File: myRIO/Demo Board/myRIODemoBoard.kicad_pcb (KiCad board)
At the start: 2 copper layers, 45.7 x 38.1 mm, 5 parts, among them U1 MXP

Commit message: Small updates to footprints, schematic, etc.
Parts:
- moved RV1 3.57 mm to (141.2, 77.2)
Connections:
- net N-000001 renamed f
- net N-0000014 renamed dp
- net N-000002 renamed e
- net N-000003 renamed d
- net N-000004 renamed c
- net N-000005 renamed b
- net N-000006 renamed a
- net N-000007 renamed g
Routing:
- net N-000009: track 22.4 -> 26.0 mm
- net +5V: track 24.4 -> 28.1 mm
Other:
- board text added: "myRIO Demo Board Rev 1.0 SK"

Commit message: Prototype Order of Rev 1.0
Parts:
- 7SEG1: value 7SEGMENTS -> 7-Segment Display
- RV1: value POT -> Potentiometer
- U1: value MXP -> NI myRIO MXP
- moved C1 19.2 mm to (143.5, 83.8), turned to 90 degrees
- moved R1 17.8 mm to (132.1, 81.3), turned to 90 degrees
- moved 7SEG1 3.81 mm to (116.8, 72.4), turned to 90 degrees
- moved RV1 3.23 mm to (143.5, 74.9), turned to 180 degrees
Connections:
- RV1 pad 3: +5V -> +3.3V
- U1 pad 1: +5V -> (no net)
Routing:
- net b: track 20.6 -> 51.5 mm
- net N-000006: track 14.8 -> 44.0 mm
- net +5V: track 28.1 -> 0.00 mm
- net N-0000018: track 36.2 -> 61.4 mm
- net dp: track 40.8 -> 15.8 mm
- net a: track 27.8 -> 52.6 mm
- net d: track 49.6 -> 25.5 mm
- net e: track 47.8 -> 26.5 mm
- net g: track 15.1 -> 33.1 mm
- net f: track 15.1 -> 30.6 mm
- net N-0000021: track 26.0 -> 12.7 mm
- net GND: track 9.20 -> 21.4 mm, vias 1 -> 0
- net c: track 31.4 -> 21.9 mm
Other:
- board text added: "Capacitor"
- board text added: "Design Real Systems, Fast"
- board text added: "NI myRIO"
- board text added: "Resistor"
- board text added: "Rev 1.0 - SK"
- board text removed: "myRIO Demo Board Rev 1.0 SK"

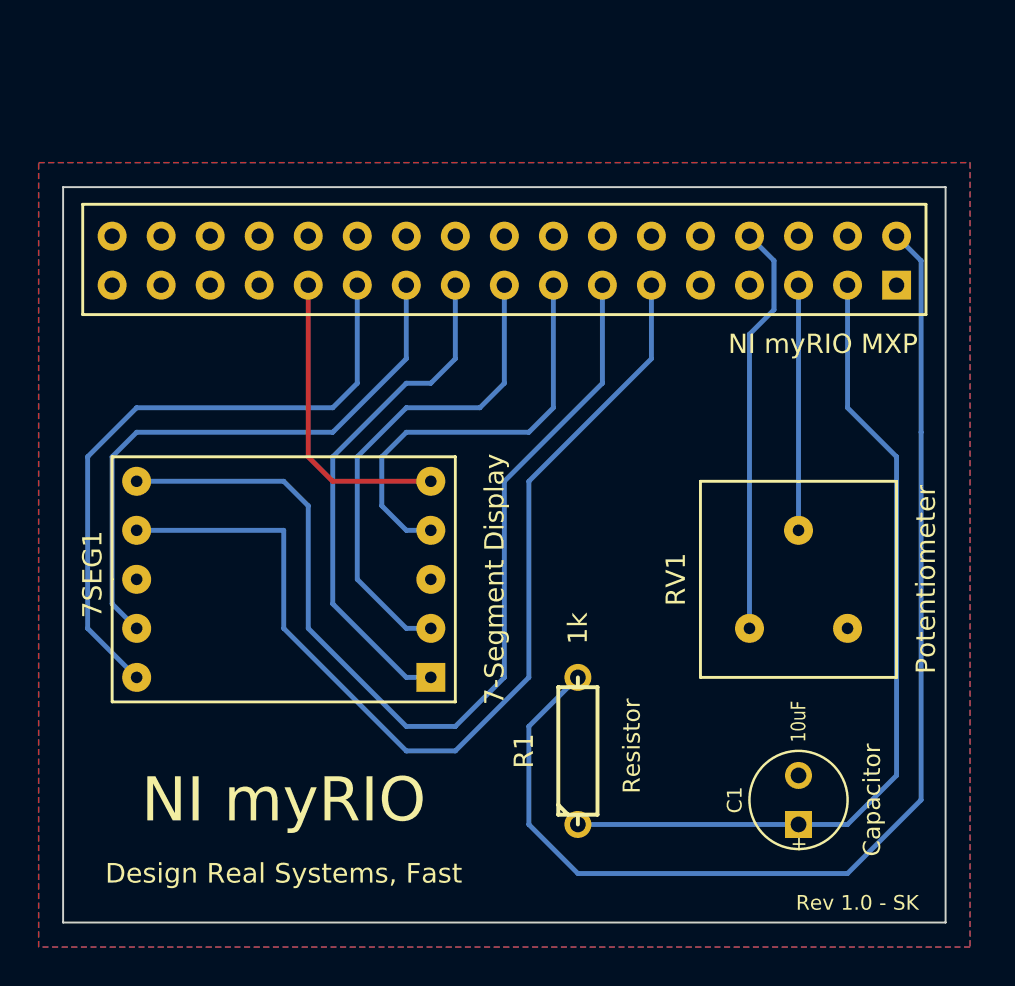
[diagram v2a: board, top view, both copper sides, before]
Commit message: Updated myRIO Demo Board to Rev 1.1. Modified component IDs for manufacturing. Adjusted silk screen.
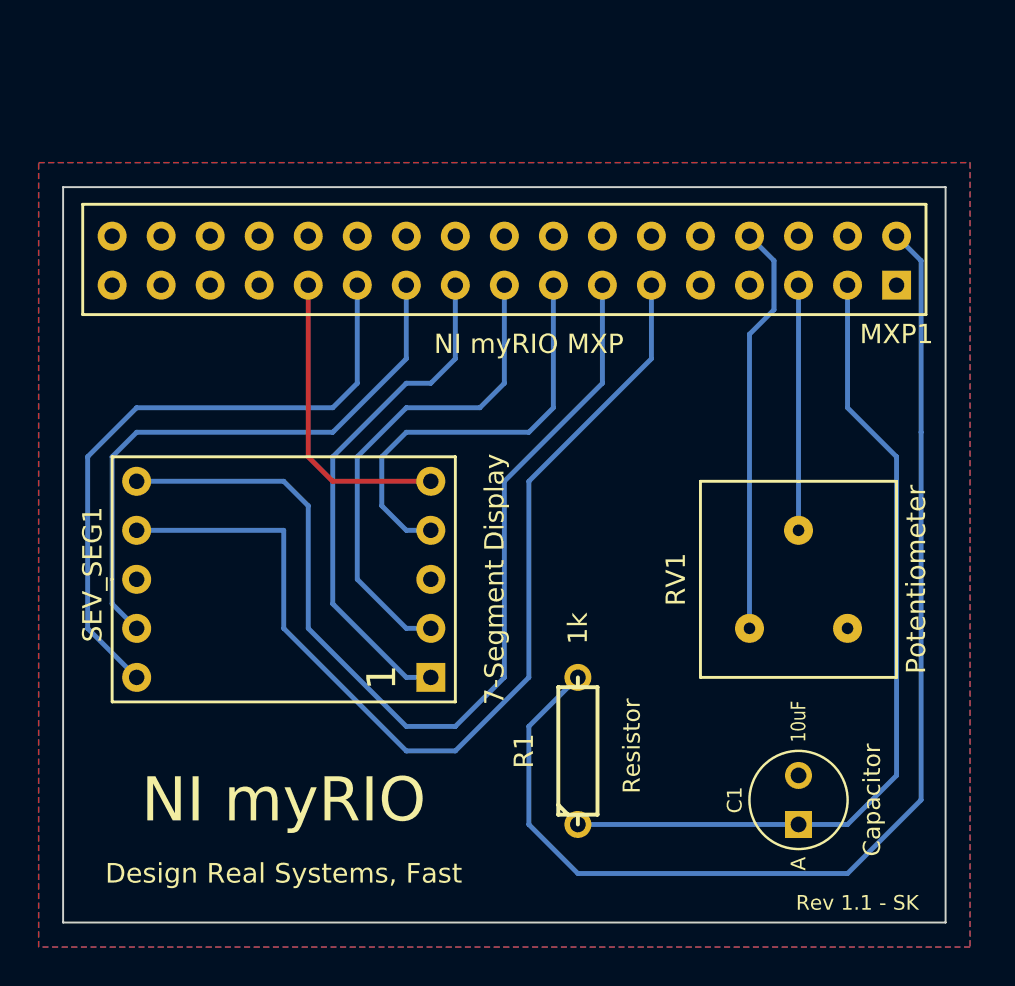
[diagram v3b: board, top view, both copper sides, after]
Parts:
- renumbered U1 to MXP1, 7SEG1 to SEV_SEG1
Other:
- board text added: "1"
- board text added: "Rev 1.1 - SK"
- board text removed: "Rev 1.0 - SK"
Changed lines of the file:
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@@
     (links 24)
     (no_connects 0)
-    (area 104.14 50.8 152.467 91.440001)
+    (area 105.359999 52.019999 151.180001 90.220001)
     (thickness 1.6)
-    (drawings 9)
+    (drawings 10)
     (tracks 72)
     (zones 0)
@@
       (effects (font (size 1 1) (thickness 0.15)))
     )
-    (fp_text value Potentiometer (at -6.604 2.54 270) (layer F.SilkS)
+    (fp_text value Potentiometer (at -6.096 2.54 270) (layer F.SilkS)
       (effects (font (size 1 1) (thickness 0.15)))
     )
@@
     )
   )
-  (module LTS-5501AB (layer F.Cu)
-    (at 116.84 72.39 90)
-    (fp_text reference 7SEG1 (at 0.254 -9.906 90) (layer F.SilkS)
-      (effects (font (size 1 1) (thickness 0.15)))
-    )
-    (fp_text value "7-Segment Display" (at 0 10.922 90) (layer F.SilkS)
-      (effects (font (size 1 1) (thickness 0.15)))
-    )
-    (fp_line (start -6.35 -8.89) (end -6.35 8.89) (layer F.SilkS) (width 0.15))
-    (fp_line (start -6.35 8.89) (end 6.35 8.89) (layer F.SilkS) (width 0.15))
-    (fp_line (start 6.35 8.89) (end 6.35 -8.89) (layer F.SilkS) (width 0.15))
-    (fp_line (start 0 -8.89) (end -6.35 -8.89) (layer F.SilkS) (width 0.15))
-    (fp_line (start 0 -8.89) (end 6.35 -8.89) (layer F.SilkS) (width 0.15))
-    (pad 1 thru_hole rect (at -5.08 7.62 90) (size 1.5 1.5) (drill 0.6)
-      (layers *.Cu *.Mask F.SilkS)
-      (net 11 e)
-    )
-    (pad 2 thru_hole circle (at -2.54 7.62 90) (size 1.5 1.5) (drill 0.6)
-      (layers *.Cu *.Mask F.SilkS)
-      (net 9 d)
-    )
-    (pad 3 thru_hole circle (at 0 7.62 90) (size 1.5 1.5) (drill 0.6)
-      (layers *.Cu *.Mask F.SilkS)
-      (net 1 +3.3V)
-    )
-    (pad 4 thru_hole circle (at 2.54 7.62 90) (size 1.5 1.5) (drill 0.6)
-      (layers *.Cu *.Mask F.SilkS)
-      (net 8 c)
-    )
-    (pad 5 thru_hole circle (at 5.08 7.62 90) (size 1.5 1.5) (drill 0.6)
-      (layers *.Cu *.Mask F.SilkS)
-      (net 10 dp)
-    )
-    (pad 6 thru_hole circle (at 5.08 -7.62 90) (size 1.5 1.5) (drill 0.6)
-      (layers *.Cu *.Mask F.SilkS)
-      (net 7 b)
-    )
-    (pad 7 thru_hole circle (at 2.54 -7.62 90) (size 1.5 1.5) (drill 0.6)
-      (layers *.Cu *.Mask F.SilkS)
-      (net 6 a)
-    )
-    (pad 8 thru_hole circle (at 0 -7.62 90) (size 1.5 1.5) (drill 0.6)
-      (layers *.Cu *.Mask F.SilkS)
-      (net 1 +3.3V)
-    )
-    (pad 9 thru_hole circle (at -2.54 -7.62 90) (size 1.5 1.5) (drill 0.6)
-      (layers *.Cu *.Mask F.SilkS)
-      (net 12 f)
-    )
-    (pad 10 thru_hole circle (at -5.08 -7.62 90) (size 1.5 1.5) (drill 0.6)
-      (layers *.Cu *.Mask F.SilkS)
-      (net 13 g)
-    )
-  )
   (module C1V5 (layer F.Cu)
     (at 143.51 83.82 90)
@@
       (effects (font (size 0.762 0.635) (thickness 0.127)))
     )
-    (fp_text user + (at -2.286 0 90) (layer F.SilkS)
-      (effects (font (size 0.762 0.762) (thickness 0.2032)))
+    (fp_text user A (at -3.302 0 90) (layer F.SilkS)
+      (effects (font (size 0.762 0.762) (thickness 0.1905)))
     )
     (fp_circle (center 0 0) (end 0.127 -2.54) (layer F.SilkS) (width 0.127))
@@
   (module MXP (layer F.Cu)
     (at 129.54 55.88)
-    (fp_text reference U1 (at 22.098 0 90) (layer F.SilkS) hide
-      (effects (font (size 1 1) (thickness 0.15)))
-    )
-    (fp_text value "NI myRIO MXP" (at 15.24 4.318) (layer F.SilkS)
+    (fp_text reference MXP1 (at 19.05 3.81) (layer F.SilkS)
+      (effects (font (size 1 1) (thickness 0.15)))
+    )
+    (fp_text value "NI myRIO MXP" (at 0 4.318) (layer F.SilkS)
       (effects (font (size 1 1) (thickness 0.15)))
     )
@@
     )
   )
-  (gr_text "Rev 1.0 - SK" (at 146.558 89.154) (layer F.SilkS)
+  (module LTS-5501AB (layer F.Cu)
+    (at 116.84 72.39 90)
+    (fp_text reference SEV_SEG1 (at 0.254 -9.906 90) (layer F.SilkS)
+      (effects (font (size 1 1) (thickness 0.15)))
+    )
+    (fp_text value "7-Segment Display" (at 0 10.922 90) (layer F.SilkS)
+      (effects (font (size 1 1) (thickness 0.15)))
+    )
+    (fp_line (start -6.35 -8.89) (end -6.35 8.89) (layer F.SilkS) (width 0.15))
+    (fp_line (start -6.35 8.89) (end 6.35 8.89) (layer F.SilkS) (width 0.15))
+    (fp_line (start 6.35 8.89) (end 6.35 -8.89) (layer F.SilkS) (width 0.15))
+    (fp_line (start 0 -8.89) (end -6.35 -8.89) (layer F.SilkS) (width 0.15))
+    (fp_line (start 0 -8.89) (end 6.35 -8.89) (layer F.SilkS) (width 0.15))
+    (pad 1 thru_hole rect (at -5.08 7.62 90) (size 1.5 1.5) (drill 0.8)
+      (layers *.Cu *.Mask F.SilkS)
+      (net 11 e)
+    )
+    (pad 2 thru_hole circle (at -2.54 7.62 90) (size 1.5 1.5) (drill 0.8)
+      (layers *.Cu *.Mask F.SilkS)
+      (net 9 d)
+    )
+    (pad 3 thru_hole circle (at 0 7.62 90) (size 1.5 1.5) (drill 0.8)
+      (layers *.Cu *.Mask F.SilkS)
+      (net 1 +3.3V)
+    )
+    (pad 4 thru_hole circle (at 2.54 7.62 90) (size 1.5 1.5) (drill 0.8)
+      (layers *.Cu *.Mask F.SilkS)
+      (net 8 c)
+    )
+    (pad 5 thru_hole circle (at 5.08 7.62 90) (size 1.5 1.5) (drill 0.8)
+      (layers *.Cu *.Mask F.SilkS)
+      (net 10 dp)
+    )
+    (pad 6 thru_hole circle (at 5.08 -7.62 90) (size 1.5 1.5) (drill 0.8)
+      (layers *.Cu *.Mask F.SilkS)
+      (net 7 b)
+    )
+    (pad 7 thru_hole circle (at 2.54 -7.62 90) (size 1.5 1.5) (drill 0.8)
+      (layers *.Cu *.Mask F.SilkS)
+      (net 6 a)
+    )
+    (pad 8 thru_hole circle (at 0 -7.62 90) (size 1.5 1.5) (drill 0.8)
+      (layers *.Cu *.Mask F.SilkS)
+      (net 1 +3.3V)
+    )
+    (pad 9 thru_hole circle (at -2.54 -7.62 90) (size 1.5 1.5) (drill 0.8)
+      (layers *.Cu *.Mask F.SilkS)
+      (net 12 f)
+    )
+    (pad 10 thru_hole circle (at -5.08 -7.62 90) (size 1.5 1.5) (drill 0.8)
+      (layers *.Cu *.Mask F.SilkS)
+      (net 13 g)
+    )
+  )
+  (gr_text 1 (at 121.92 77.47 90) (layer F.SilkS)
+    (effects (font (size 1.5 1.5) (thickness 0.3)))
+  )
+  (gr_text "Rev 1.1 - SK" (at 146.558 89.154) (layer F.SilkS)
     (effects (font (size 0.762 0.762) (thickness 0.0762)))
   )

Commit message: Updated BOM and component IDs to work better with Screaming Circuits  parser
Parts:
- renumbered SEV_SEG1 to SEG1
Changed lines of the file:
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@@
     (links 24)
     (no_connects 0)
-    (area 105.359999 52.019999 151.180001 90.220001)
+    (area 104.14 50.8 152.400001 91.440001)
     (thickness 1.6)
     (drawings 10)
@@
   (module LTS-5501AB (layer F.Cu)
     (at 116.84 72.39 90)
-    (fp_text reference SEV_SEG1 (at 0.254 -9.906 90) (layer F.SilkS)
-      (effects (font (size 1 1) (thickness 0.15)))
-    )
+    (fp_text reference SEG1 (at 0.254 -9.906 90) (layer F.SilkS)
+      (effects (font (size 1 1) (thickness 0.15)))
+    )

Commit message: Updated R1 to 200k in schematic, BOM and silkscreen Generated new gerbers.
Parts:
- R1: value 1k -> 200k
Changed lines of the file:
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@@
       (effects (font (size 1 1) (thickness 0.2032)))
     )
-    (fp_text value 1k (at 6.35 0 90) (layer F.SilkS)
+    (fp_text value 200k (at 7.366 0 90) (layer F.SilkS)
       (effects (font (size 1 1) (thickness 0.2032)))
     )

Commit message: Reved to 1.2
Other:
- board text added: "Rev 1.2 - SK"
- board text removed: "Rev 1.1 - SK"
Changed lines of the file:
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@@
     (effects (font (size 1.5 1.5) (thickness 0.3)))
   )
-  (gr_text "Rev 1.1 - SK" (at 146.558 89.154) (layer F.SilkS)
+  (gr_text "Rev 1.2 - SK" (at 146.558 89.154) (layer F.SilkS)
     (effects (font (size 0.762 0.762) (thickness 0.0762)))
   )
